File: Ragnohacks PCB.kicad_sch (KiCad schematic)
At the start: 38 parts, among them J1 Conn_01x02, J2 Conn_01x18, J3 Conn_01x18, J4 USB_A, J5 USB_C_Receptacle_USB2.0_16P, SW1 SW_Push, U1 RP2040, U2 W25Q128JVS, U3 LD1117S33TR_SOT223, U4 USBLC6-2P6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

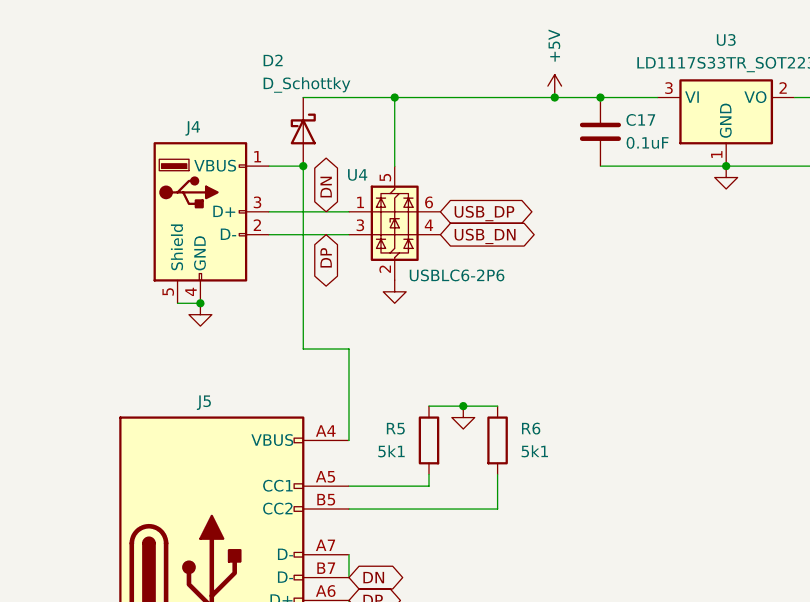
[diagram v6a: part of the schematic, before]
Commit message: Swap USB pins
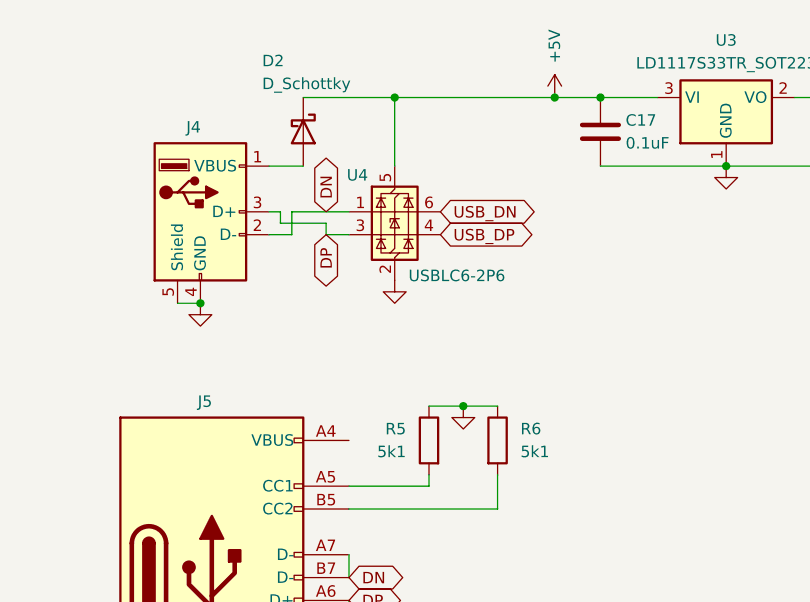
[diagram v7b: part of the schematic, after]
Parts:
- J5: LCSC (none) -> C2765186
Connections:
- net DN: now also J4.2 (D-); no longer J4.3 (D+)
- net DP: now also J4.3 (D+); no longer J4.2 (D-)
- net USB_DN: now also U4.6 (I/O1); no longer U4.4 (I/O2)
- net USB_DP: now also U4.4 (I/O2); no longer U4.6 (I/O1)
- net at J5.A4 (VBUS), J5.A9 (VBUS), J5.B4 (VBUS)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: no longer D2.2 (A), J4.1 (VBUS)
- new net: D2.2 (A), J4.1 (VBUS)
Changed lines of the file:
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@@
 	)
 	(junction
-		(at 163.83 68.58)
-		(diameter 0)
-		(color 0 0 0 0)
-	)
-	(junction
 		(at 29.21 95.25)
 		(diameter 0)
@@
 	(wire
 		(pts
+			(xy 166.37 76.2) (xy 168.91 76.2)
+		)
+		(stroke
+			(width 0)
+			(type default)
+		)
+	)
+	(wire
+		(pts
 			(xy 173.99 60.96) (xy 173.99 68.58)
 		)
@@
 	(wire
 		(pts
-			(xy 30.48 49.53) (xy 43.18 49.53)
+			(xy 162.56 73.66) (xy 168.91 73.66)
 		)
 		(stroke
@@
 	(wire
 		(pts
-			(xy 243.84 68.58) (xy 243.84 69.85)
+			(xy 30.48 49.53) (xy 43.18 49.53)
 		)
 		(stroke
@@
 	(wire
 		(pts
-			(xy 195.58 24.13) (xy 182.88 24.13)
+			(xy 243.84 68.58) (xy 243.84 69.85)
 		)
 		(stroke
@@
 	(wire
 		(pts
-			(xy 45.72 115.57) (xy 53.34 115.57)
+			(xy 195.58 24.13) (xy 182.88 24.13)
 		)
 		(stroke
@@
 	(wire
 		(pts
-			(xy 78.74 177.8) (xy 78.74 179.07)
+			(xy 45.72 115.57) (xy 53.34 115.57)
 		)
 		(stroke
@@
 	(wire
 		(pts
-			(xy 78.74 168.91) (xy 78.74 170.18)
+			(xy 78.74 177.8) (xy 78.74 179.07)
 		)
 		(stroke
@@
 	(wire
 		(pts
-			(xy 168.91 88.9) (xy 163.83 88.9)
+			(xy 78.74 168.91) (xy 78.74 170.18)
 		)
 		(stroke
@@
 	(wire
 		(pts
-			(xy 160.02 76.2) (xy 168.91 76.2)
+			(xy 160.02 76.2) (xy 162.56 76.2)
 		)
 		(stroke
@@
 	(wire
 		(pts
-			(xy 163.83 88.9) (xy 163.83 68.58)
+			(xy 161.29 73.66) (xy 161.29 74.93)
 		)
 		(stroke
@@
 	(wire
 		(pts
-			(xy 160.02 73.66) (xy 168.91 73.66)
+			(xy 144.78 24.13) (xy 157.48 24.13)
 		)
 		(stroke
@@
 	(wire
 		(pts
-			(xy 144.78 24.13) (xy 157.48 24.13)
+			(xy 161.29 74.93) (xy 166.37 74.93)
 		)
 		(stroke
@@
 	(wire
 		(pts
-			(xy 168.91 99.06) (xy 168.91 88.9)
+			(xy 149.86 83.82) (xy 152.4 83.82)
 		)
 		(stroke
@@
 	(wire
 		(pts
-			(xy 149.86 83.82) (xy 152.4 83.82)
+			(xy 30.48 54.61) (xy 30.48 49.53)
 		)
 		(stroke
@@
 	(wire
 		(pts
-			(xy 30.48 54.61) (xy 30.48 49.53)
+			(xy 196.85 60.96) (xy 191.77 60.96)
 		)
 		(stroke
@@
 	(wire
 		(pts
-			(xy 196.85 60.96) (xy 191.77 60.96)
+			(xy 119.38 24.13) (xy 106.68 24.13)
 		)
 		(stroke
@@
 	(wire
 		(pts
-			(xy 119.38 24.13) (xy 106.68 24.13)
+			(xy 40.64 33.02) (xy 53.34 33.02)
 		)
 		(stroke
@@
 	(wire
 		(pts
-			(xy 40.64 33.02) (xy 53.34 33.02)
+			(xy 16.51 49.53) (xy 20.32 49.53)
 		)
 		(stroke
@@
 	(wire
 		(pts
-			(xy 16.51 49.53) (xy 20.32 49.53)
+			(xy 166.37 74.93) (xy 166.37 76.2)
 		)
 		(stroke
@@
 	(wire
 		(pts
+			(xy 162.56 76.2) (xy 162.56 73.66)
+		)
+		(stroke
+			(width 0)
+			(type default)
+		)
+	)
+	(wire
+		(pts
+			(xy 160.02 73.66) (xy 161.29 73.66)
+		)
+		(stroke
+			(width 0)
+			(type default)
+		)
+	)
+	(wire
+		(pts
 			(xy 177.8 95.25) (xy 181.61 95.25)
 		)
@@
 	(global_label "USB_DN"
 		(shape bidirectional)
-		(at 179.07 76.2 0)
+		(at 179.07 73.66 0)
 		(fields_autoplaced yes)
 		(effects
@@
 		)
 		(property "Intersheetrefs" "${INTERSHEET_REFS}"
-			(at 190.5446 76.2 0)
+			(at 190.5446 73.66 0)
 			(effects
 				(font
@@
 	(global_label "USB_DP"
 		(shape bidirectional)
-		(at 179.07 73.66 0)
+		(at 179.07 76.2 0)
 		(fields_autoplaced yes)
 		(effects
@@
 		)
 		(property "Intersheetrefs" "${INTERSHEET_REFS}"
-			(at 190.4841 73.66 0)
+			(at 190.4841 76.2 0)
 			(effects
 				(font
@@
 			(at 153.67 114.3 0)
 			(effects
+				(font
+					(size 1.27 1.27)
+				)
+				(hide yes)
+			)
+		)
+		(property "MPN" ""
+			(at 153.67 114.3 0)
+			(effects
+				(font
+					(size 1.27 1.27)
+				)
+				(hide yes)
+			)
+		)
+		(property "LCSC" "C2765186"
+			(at 153.67 114.3 0)
+			(effects
